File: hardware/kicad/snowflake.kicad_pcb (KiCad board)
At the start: 2 copper layers, 123.3 x 86 mm, 60 parts

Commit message: Wired the keyboard
Wired the keyboard based on the previous changes.
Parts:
- D1, D10, D11, D12, D13, D14, D15, D16, D17, D18, D2, D3, D4, D5, D6, D7, D8, D9: moved to F.Cu
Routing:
- net (no net): track 262.1 -> 0.00 mm
- net P15: track 88.5 -> 261.7 mm
- net P18: track 88.5 -> 226.0 mm
- net P19: track 118.0 -> 253.5 mm
- net P20: track 118.0 -> 221.6 mm
- net P6: track 61.0 -> 147.2 mm
- net P7: track 30.5 -> 115.1 mm
- net P21: track 118.0 -> 200.2 mm
- net GND: track 0.00 -> 77.8 mm
- net P5: track 61.0 -> 131.0 mm
- net P2: track 0.00 -> 69.5 mm
- net P4: track 61.0 -> 120.9 mm
- net RST: track 0.00 -> 58.6 mm
- net P3: track 0.00 -> 51.7 mm
- net VCC: track 0.00 -> 46.9 mm
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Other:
- net class Default removed

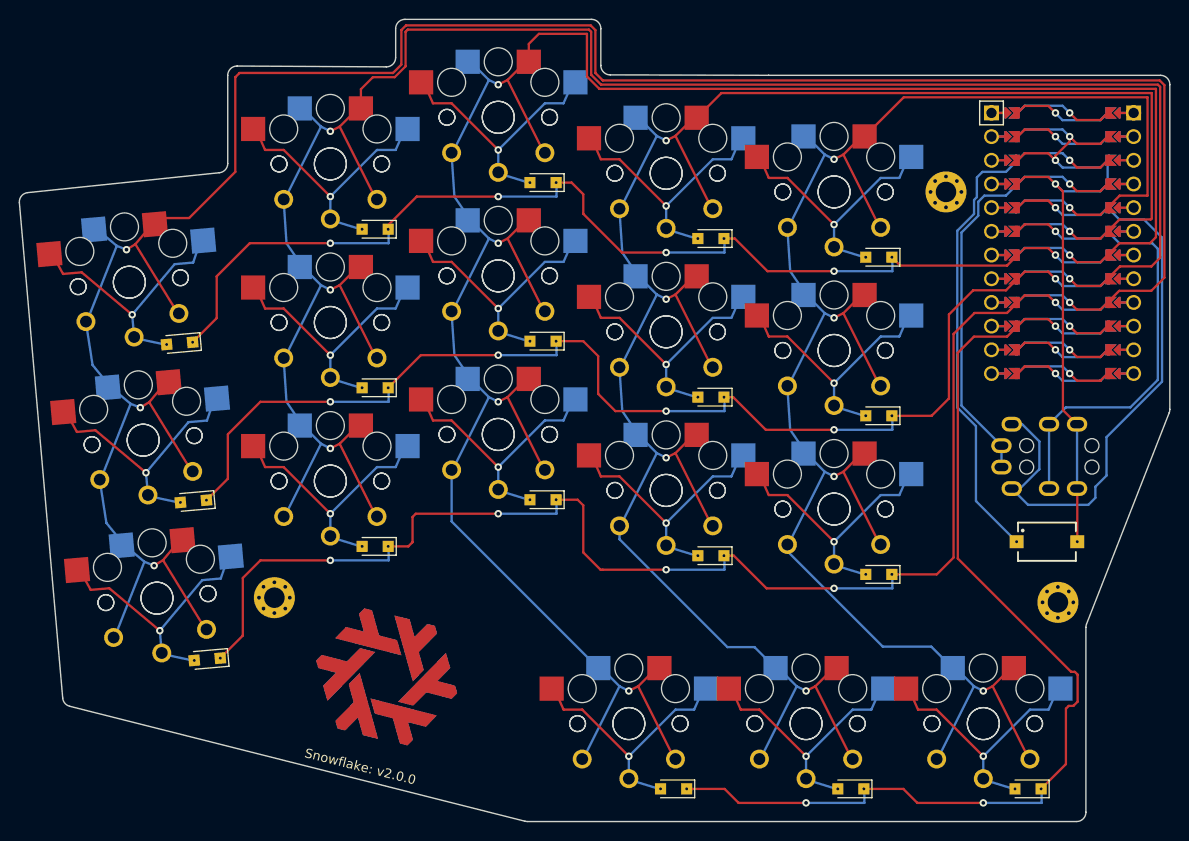
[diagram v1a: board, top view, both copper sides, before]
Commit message: fix: TRRS connector being to close to the edge (#25)
some TRRS connectors with big husles would get stuck on the edge and would
not be able to able to go in all the way. This commit resolves that issue.

closes #24
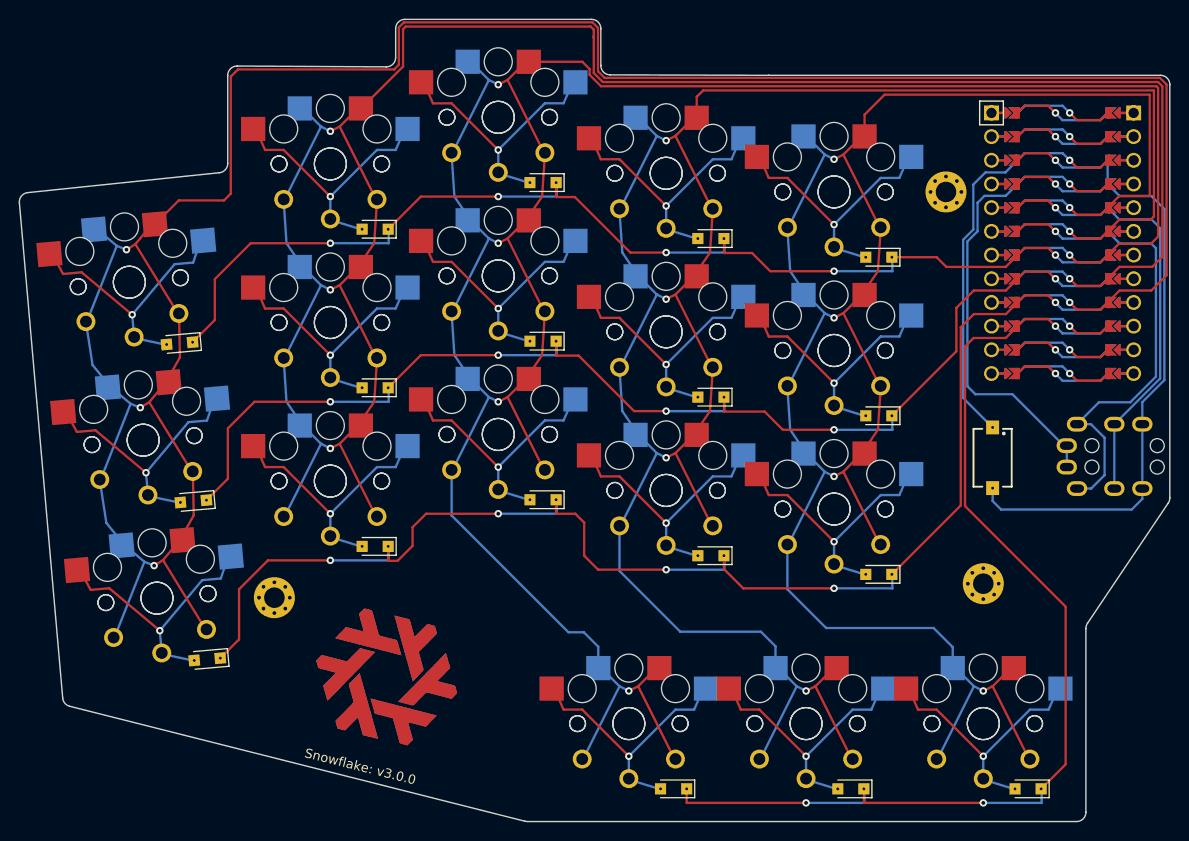
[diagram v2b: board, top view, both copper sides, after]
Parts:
- moved S1 10.7 mm to (189.6, 85.0), turned to -90 degrees
- moved _2 8.25 mm to (188.6, 98.5)
- moved TRRS1 7.00 mm to (208.8, 86.0)
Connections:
- TRRS1 pad 2: P2 -> P3
- TRRS1 pad 3: P3 -> P2
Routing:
- net P2: track 69.5 -> 47.4 mm
- net P21: track 200.2 -> 221.2 mm
- net P20: track 221.6 -> 242.1 mm
- net P15: track 261.7 -> 279.0 mm
- net GND: track 77.8 -> 92.8 mm
- net P18: track 226.0 -> 241.0 mm
- net RST: track 58.6 -> 44.5 mm
- net P19: track 253.5 -> 264.1 mm
- net VCC: track 46.9 -> 51.8 mm
- net P5: track 131.0 -> 128.2 mm
- net P6: track 147.2 -> 146.5 mm
- net P3: track 51.7 -> 52.3 mm
- net P7: track 115.1 -> 114.5 mm
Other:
- outline, holes or cut-outs redrawn
- board text added: "Snowflake: v3.0.0"
- board text removed: "Snowflake: v2.0.0"

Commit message: feat!: added a 3 way jumpers (#28)
So while building the firmware for version 2, I found that I could not
easily build the firmware deterministically as a write to the EPROM is
required the first time you flash the firmware. It would be nice to
have a hardware option to decide what side it is. We solder anything
into one of two possible configurations anyways, thus this does not
make the PCB less flexible.

I would argue that this makes it more flexible as you don't need this
pin to get a working keyboard. You can still do it the old way if you
want to, although you'd have to change at most 5 lines in the firmware.
It just allows the keyboard to see what side it is without writing to
the EPROM the first time. Making the firmware process fully
reproducible.

I also added the same 3 way jumper to the back of the TRRS connector.
This way you have a resistor on each side pulling either the clock
or data line up to high.

BREAKING CHANGE: moved the top mounting hole so any previous cases are
incompatible. Here it provides better support and it is less in the way.

BREAKING CHANGE: Changed the order of the pins on the TRRS connector.
This results in a loss of interoperability to communicate with older
versions. This needed to be done to make routing easier, and cleaner.

Since this release already has a breaking change, I do not see the
problem with adding more as this version is already completely
incompatible with the previous release.

Closes #26: "Make jumpers to allow for assigning something to the left
or right side".
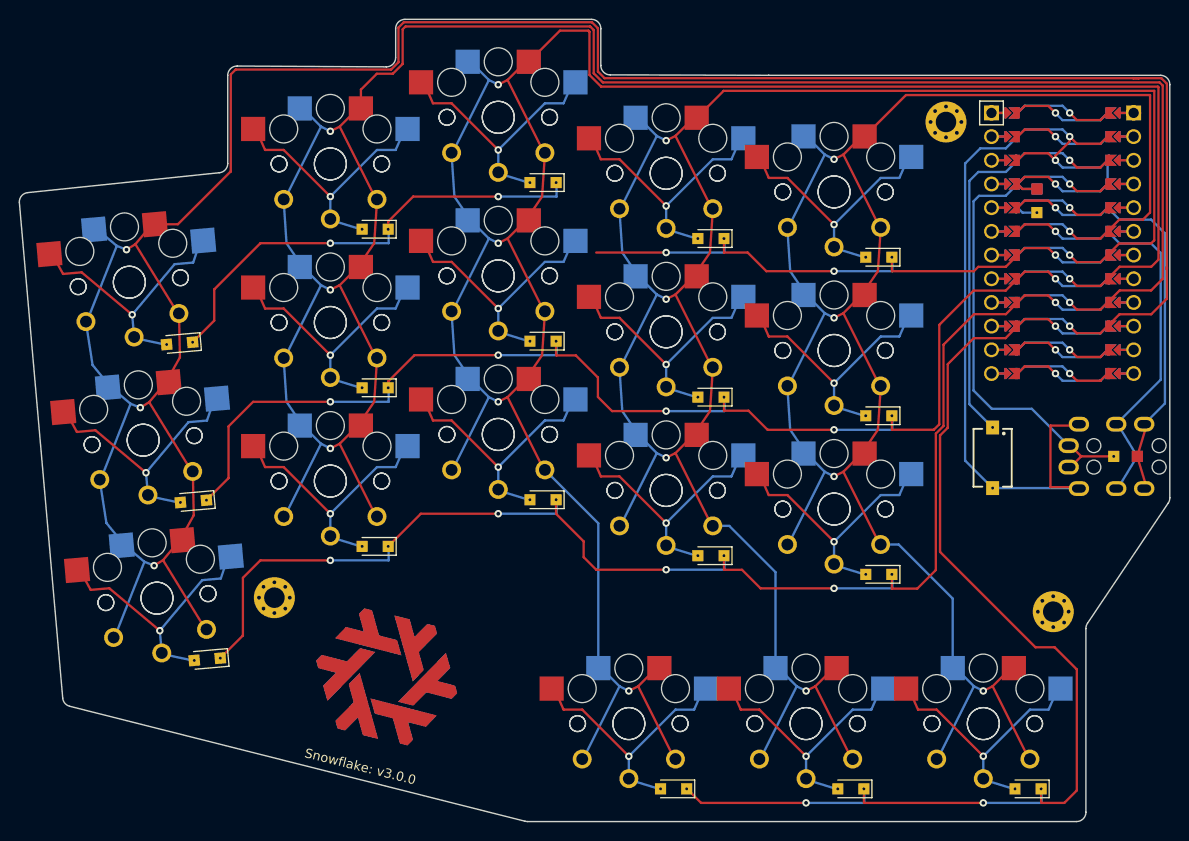
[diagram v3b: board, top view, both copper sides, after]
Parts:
- added threeWayJumper1: Jumper, Jumper_1TH_2SMD, F.Cu at (194.3, 57.4)
- added threeWayJumper2: Jumper, Jumper_1TH_2SMD, F.Cu at (203.8, 84.8)
- moved _2 8.08 mm to (196.1, 101.5)
- moved _1 7.50 mm to (184.6, 49.0)
- moved TRRS1 0.20 mm to (209.0, 86.0)
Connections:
- S10 pad 1: P19 -> P18
- S11 pad 1: P20 -> P19
- S12 pad 1: P20 -> P19
- S13 pad 1: P20 -> P19
- S14 pad 1: P21 -> P20
- S15 pad 1: P21 -> P20
- S16 pad 1: P21 -> P20
- S17 pad 1: P19 -> P18
- S18 pad 1: P20 -> P19
- S19 pad 1: P21 -> P20
- S2 pad 1: P15 -> P14
- S20 pad 1: P15 -> P14
- S21 pad 1: P15 -> P14
- S22 pad 1: P15 -> P14
- S23 pad 1: P18 -> P15
- S24 pad 1: P18 -> P15
- S25 pad 1: P18 -> P15
- S26 pad 1: P19 -> P18
- S27 pad 1: P19 -> P18
- S28 pad 1: P19 -> P18
- S29 pad 1: P20 -> P19
- S3 pad 1: P15 -> P14
- S30 pad 1: P20 -> P19
- S31 pad 1: P20 -> P19
- S32 pad 1: P21 -> P20
- S33 pad 1: P21 -> P20
- S34 pad 1: P21 -> P20
- S35 pad 1: P19 -> P18
- S36 pad 1: P20 -> P19
- S37 pad 1: P21 -> P20
- S4 pad 1: P15 -> P14
- S5 pad 1: P18 -> P15
- S6 pad 1: P18 -> P15
- S7 pad 1: P18 -> P15
- S8 pad 1: P19 -> P18
- S9 pad 1: P19 -> P18
- TRRS1 pad 2: P3 -> GND
- TRRS1 pad 3: P2 -> P3
- TRRS1 pad 4: GND -> P2
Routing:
- net P14: track 10.9 -> 281.1 mm, vias 1 -> 4
- net P21: track 221.2 -> 13.2 mm, vias 5 -> 1
- net P15: track 279.0 -> 244.4 mm
- net P20: track 242.1 -> 212.2 mm
- net P19: track 264.1 -> 235.2 mm
- net P18: track 241.0 -> 266.7 mm, vias 4 -> 5
- net GND: track 92.8 -> 104.7 mm
- net P7: track 114.5 -> 122.5 mm
- net P5: track 128.2 -> 135.5 mm
- net P4: track 121.3 -> 114.1 mm
- net P3: track 52.3 -> 45.6 mm
- net VCC: track 51.8 -> 58.0 mm
- net P2: track 47.4 -> 46.5 mm
- net P6: track 146.5 -> 147.2 mm

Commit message: fix: saw a single wire that was not wired up
There was a missing connection between two keys the PCB would not have worked
without this fix.
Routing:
- net P4: track 114.1 -> 123.9 mm
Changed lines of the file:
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@@
 		(0 "F.Cu" signal)
 		(2 "B.Cu" signal)
-		(9 "F.Adhes" user)
-		(11 "B.Adhes" user)
+		(9 "F.Adhes" user "F.Adhesive")
+		(11 "B.Adhes" user "B.Adhesive")
 		(13 "F.Paste" user)
 		(15 "B.Paste" user)
-		(5 "F.SilkS" user)
-		(7 "B.SilkS" user)
+		(5 "F.SilkS" user "F.Silkscreen")
+		(7 "B.SilkS" user "B.Silkscreen")
 		(1 "F.Mask" user)
 		(3 "B.Mask" user)
-		(17 "Dwgs.User" user)
-		(19 "Cmts.User" user)
-		(21 "Eco1.User" user)
-		(23 "Eco2.User" user)
+		(17 "Dwgs.User" user "User.Drawings")
+		(19 "Cmts.User" user "User.Comments")
+		(21 "Eco1.User" user "User.Eco1")
+		(23 "Eco2.User" user "User.Eco2")
 		(25 "Edge.Cuts" user)
 		(27 "Margin" user)
-		(31 "F.CrtYd" user)
-		(29 "B.CrtYd" user)
+		(31 "F.CrtYd" user "F.Courtyard")
+		(29 "B.CrtYd" user "B.Courtyard")
 		(35 "F.Fab" user)
 		(33 "B.Fab" user)
@@
 		)
 		(pad "" np_thru_hole circle
-			(at -5.000001 -3.75)
+			(at -5.000002 -3.75)
 			(size 3 3)
 			(drill 3)
@@
 		)
 		(pad "" np_thru_hole circle
-			(at -5.000001 -3.75)
+			(at -5.000002 -3.75)
 			(size 3 3)
 			(drill 3)
@@
 		)
 		(pad "" np_thru_hole circle
-			(at -5.000001 -3.75)
+			(at -5.000002 -3.75)
 			(size 3 3)
 			(drill 3)
@@
 	)
 	(segment
-		(start 147.087258 62.950428)
-		(end 154.587258 62.950428)
+		(start 103.823203 72.562378)
+		(end 106.14 70.245581)
 		(width 0.25)
 		(layer "F.Cu")
@@
 	)
 	(segment
-		(start 103.823203 72.562378)
-		(end 106.14 70.245581)
+		(start 196.319357 63.232649)
+		(end 195.553357 62.466649)
 		(width 0.25)
 		(layer "F.Cu")
@@
 	)
 	(segment
-		(start 196.319357 63.232649)
-		(end 195.553357 62.466649)
+		(start 142.787258 55.450428)
+		(end 142.787258 56.94)
 		(width 0.25)
 		(layer "F.Cu")
@@
 	)
 	(segment
+		(start 147.6 58.94)
+		(end 147.6 61.610428)
+		(width 0.25)
+		(layer "F.Cu")
+		(net 17)
+	)
+	(segment
 		(start 160.787258 62.947258)
 		(end 160.79 62.95)
@@
 	)
 	(segment
+		(start 147.6 61.610428)
+		(end 148.94 62.950428)
+		(width 0.25)
+		(layer "F.Cu")
+		(net 17)
+	)
+	(segment
 		(start 192.261258 63.220428)
 		(end 191.001686 64.48)
@@
 	)
 	(segment
+		(start 142.787258 56.94)
+		(end 145.6 56.94)
+		(width 0.25)
+		(layer "F.Cu")
+		(net 17)
+	)
+	(segment
+		(start 145.6 56.94)
+		(end 147.6 58.94)
+		(width 0.25)
+		(layer "F.Cu")
+		(net 17)
+	)
+	(segment
 		(start 165.330428 64.950428)
 		(end 172.587258 64.950428)
@@
 		(width 0.25)
 		(layer "F.Cu")
+		(net 17)
+	)
+	(segment
+		(start 148.94 62.950428)
+		(end 154.587258 62.950428)
+		(width 0.25)
+		(layer "F.Cu")
